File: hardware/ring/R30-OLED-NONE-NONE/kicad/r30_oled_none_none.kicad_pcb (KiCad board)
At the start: 2 copper layers, 43 x 18 mm, 32 parts, among them J1 USB4215-class 16P TH stakes, Q1 SI2301 P-FET, Q2 2N7002 gate driver, SW1 5mm 200gf dome, U1 ESP32-C3-MINI-1-N4, U2 PAW3204DB-TJ3L, U3 TP4054, U4 RT9080-33GJ5

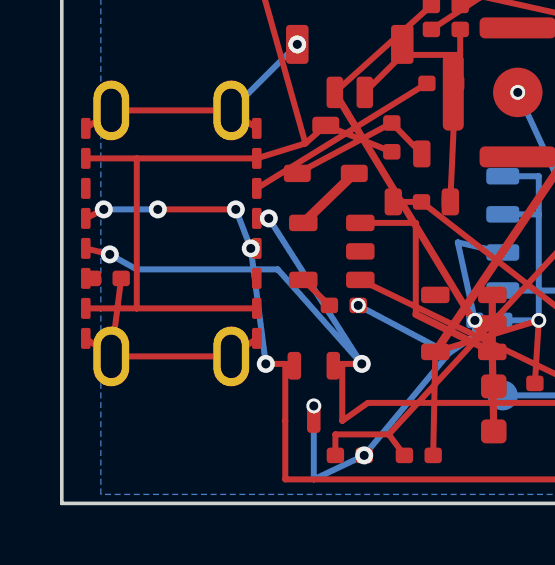
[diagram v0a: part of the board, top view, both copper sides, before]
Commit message: fix(r30): ease cc2 pulldown clearance
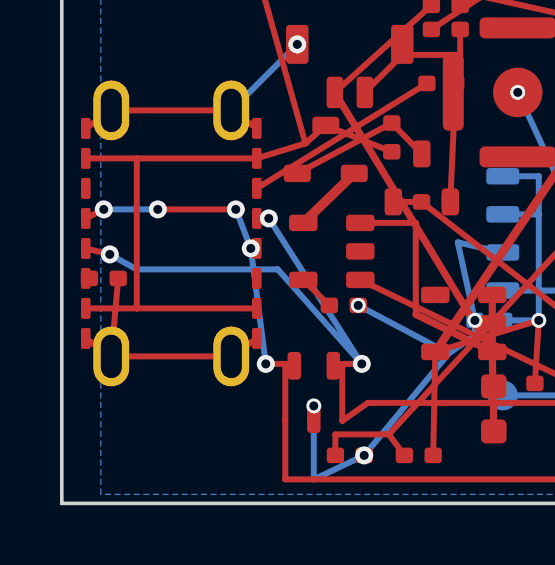
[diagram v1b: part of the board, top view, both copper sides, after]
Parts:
- moved R2B 0.10 mm to (100.4, 101.5)
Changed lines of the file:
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@@
   (footprint "Resistor_SMD:R_0402_1005Metric"
     (layer "F.Cu")
-    (at 100.500 101.500 0)
+    (at 100.400 101.500 0)
     (property "Reference" "R2B" (at 0 -1.05 0) (layer "F.Fab") (effects (font (size 0.6 0.6) (thickness 0.09))))
     (property "Value" "5.1k" (at 0 1.05 0) (layer "F.Fab") (effects (font (size 0.55 0.55) (thickness 0.08))))
@@
   (segment (start 119.600 108.200) (end 119.600 106.350) (width 0.20) (layer "F.Cu") (net 17))
   (segment (start 105.500 98.500) (end 111.170 95.000) (width 0.20) (layer "F.Cu") (net 18))
-  (segment (start 99.800 101.500) (end 100.020 101.500) (width 0.20) (layer "F.Cu") (net 19))
+  (segment (start 99.800 101.500) (end 99.920 101.500) (width 0.20) (layer "F.Cu") (net 19))
   (segment (start 108.950 101.550) (end 116.100 105.000) (width 0.20) (layer "F.Cu") (net 20))
   (segment (start 112.280 92.400) (end 113.000 92.100) (width 0.20) (layer "F.Cu") (net 21))
@@
   (segment (start 112.130 95.000) (end 111.950 98.950) (width 0.20) (layer "F.Cu") (net 1))
   (segment (start 108.880 102.400) (end 111.900 104.000) (width 0.20) (layer "B.Cu") (net 1))
-  (segment (start 100.980 101.500) (end 100.650 104.100) (width 0.20) (layer "F.Cu") (net 1))
+  (segment (start 100.880 101.500) (end 100.650 104.100) (width 0.20) (layer "F.Cu") (net 1))
   (segment (start 109.080 107.400) (end 111.900 104.000) (width 0.20) (layer "B.Cu") (net 1))
   (segment (start 111.900 104.000) (end 112.770 103.400) (width 0.20) (layer "B.Cu") (net 1))

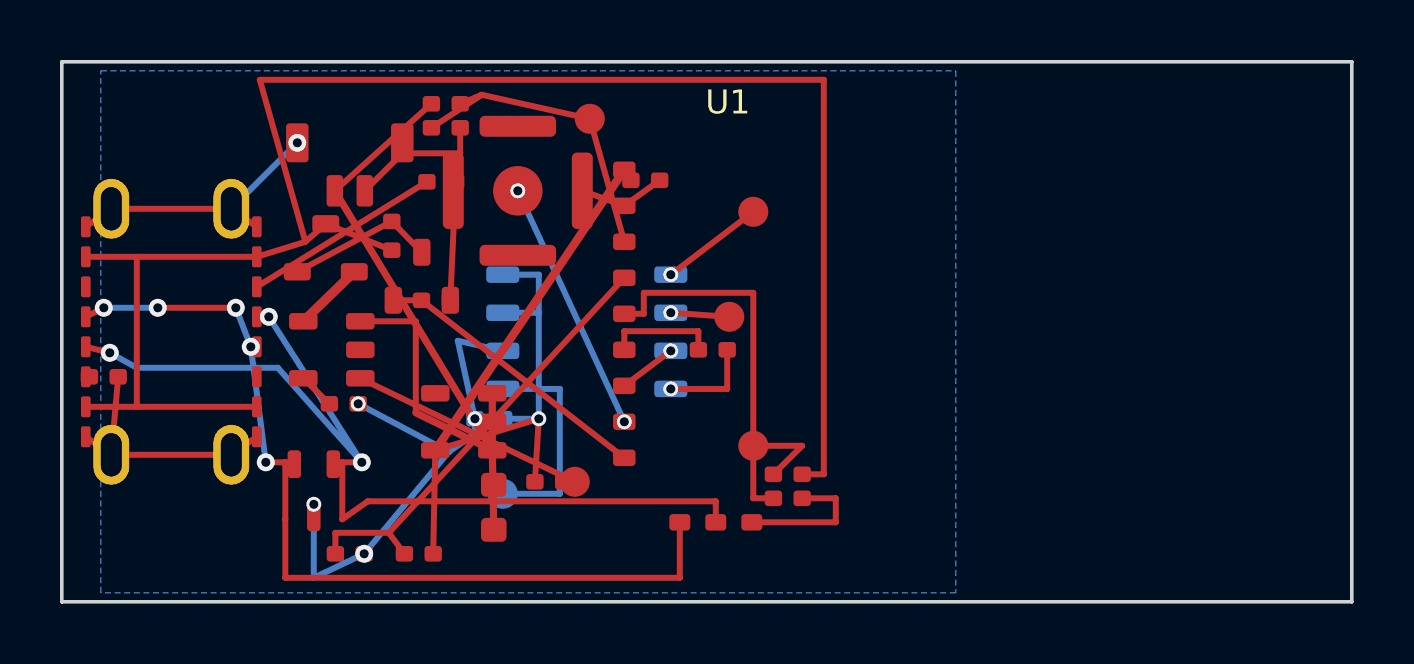
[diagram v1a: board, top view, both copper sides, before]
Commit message: fix(r30): ease dome switch clearance
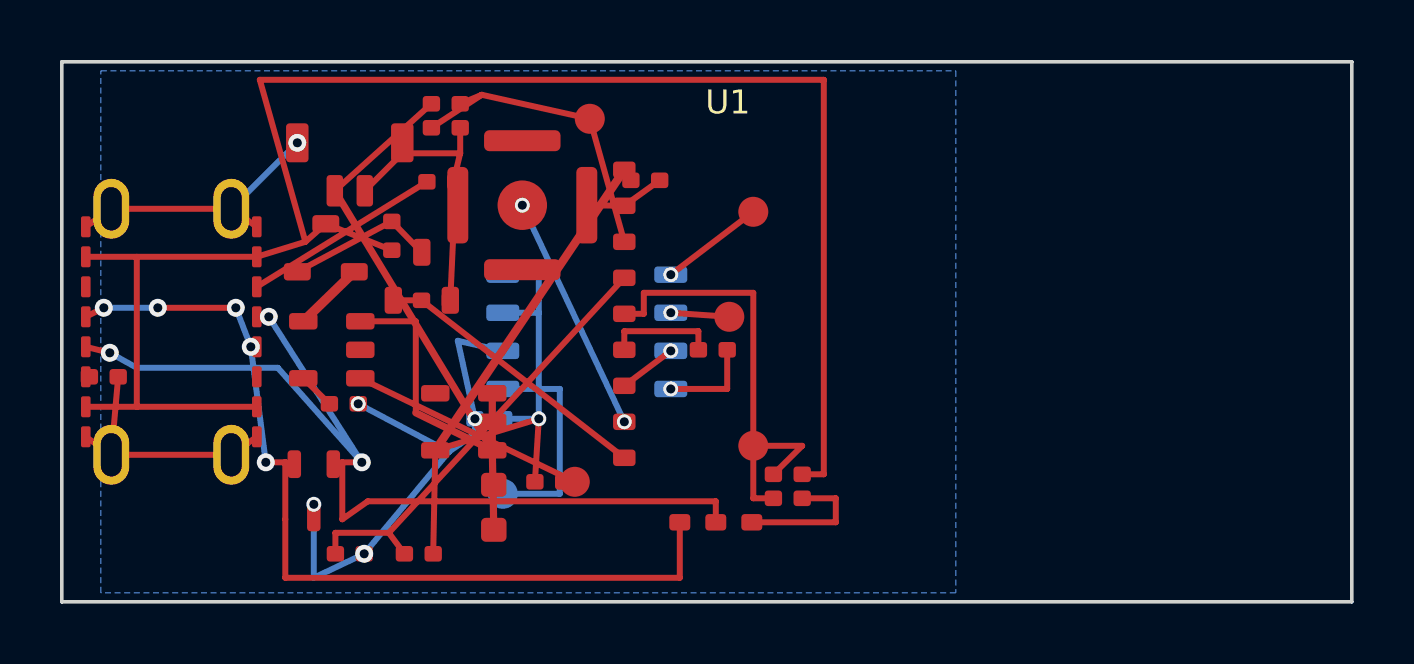
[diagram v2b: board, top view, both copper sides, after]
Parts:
- moved SW1 0.50 mm to (114.3, 95.8)
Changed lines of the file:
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@@
   (footprint "PowerFinger_Ring:Snap_Dome_5mm_TwoPad_Serviceable"
     (layer "F.Cu")
-    (at 114.200 95.300 0)
+    (at 114.350 95.780 0)
     (descr "5 mm metal snap dome contacts; accessible click zone")
     (property "Reference" "SW1" (at 0 -3.05 0) (layer "F.Fab") (effects (font (size 0.75 0.75) (thickness 0.11))))
@@
   (segment (start 124.800 106.350) (end 122.000 106.350) (width 0.20) (layer "F.Cu") (net 1))
   (segment (start 118.930 94.950) (end 117.750 95.800) (width 0.20) (layer "F.Cu") (net 1))
-  (segment (start 116.350 95.300) (end 117.750 95.800) (width 0.20) (layer "F.Cu") (net 1))
+  (segment (start 116.500 95.780) (end 117.750 95.800) (width 0.20) (layer "F.Cu") (net 1))
   (segment (start 114.770 105.000) (end 114.900 102.900) (width 0.20) (layer "F.Cu") (net 5))
   (segment (start 115.730 105.000) (end 116.100 105.000) (width 0.20) (layer "F.Cu") (net 20))
@@
   (segment (start 119.300 99.365) (end 121.250 99.500) (width 0.20) (layer "F.Cu") (net 13))
   (segment (start 119.300 98.095) (end 122.050 96.000) (width 0.20) (layer "F.Cu") (net 14))
-  (segment (start 114.200 95.300) (end 117.750 103.000) (width 0.20) (layer "B.Cu") (net 15))
+  (segment (start 114.350 95.780) (end 117.750 103.000) (width 0.20) (layer "B.Cu") (net 15))
   (segment (start 99.800 100.500) (end 100.600 100.700) (width 0.20) (layer "F.Cu") (net 16))
   (segment (start 100.600 100.700) (end 101.500 101.200) (width 0.20) (layer "B.Cu") (net 16))
@@
   (via (at 102.200 99.200) (size 0.60) (drill 0.30) (layers "F.Cu" "B.Cu") (net 17))
   (via (at 104.800 99.200) (size 0.60) (drill 0.30) (layers "F.Cu" "B.Cu") (net 17))
-  (via (at 114.200 95.300) (size 0.50) (drill 0.30) (layers "F.Cu" "B.Cu") (net 15))
+  (via (at 114.350 95.780) (size 0.50) (drill 0.30) (layers "F.Cu" "B.Cu") (net 15))
   (via (at 117.750 103.000) (size 0.50) (drill 0.30) (layers "F.Cu" "B.Cu") (net 15))
 )

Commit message: feat(r30): cut service hardware blockers
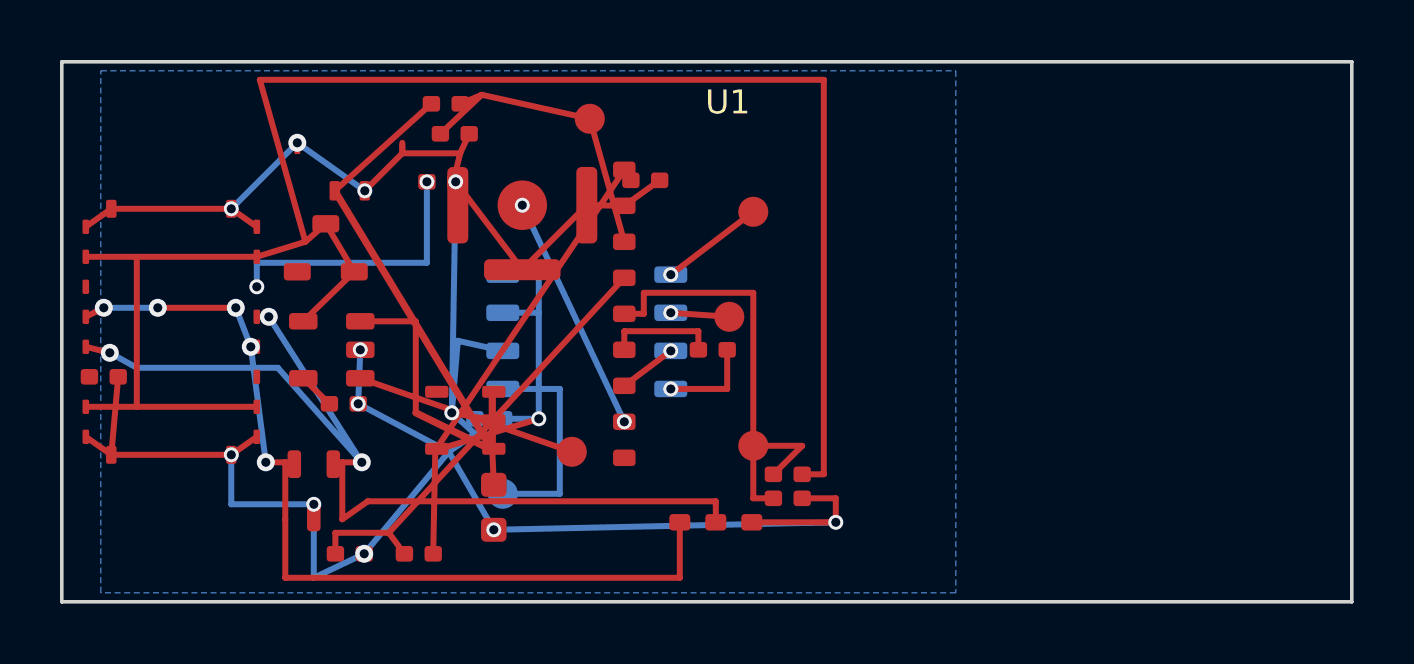
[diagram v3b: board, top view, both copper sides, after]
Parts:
- removed Q2: 2N7002 gate driver, Package_TO_SOT_SMD:SOT-23
- removed R11, R4, R6: 100k, Resistor_SMD:R_0402_1005Metric
- J1: value USB4215-class 16P TH stakes -> off-board USB service pads; footprint PowerFinger_Ring:USB_C_Receptacle_GCT_USB4215_Class_16P_TH_Stakes -> PowerFinger_Ring:Offboard_USB_Service_SameNet
- J_BAT: value SM02B-SRSS-TB class -> off-board battery service pads; footprint PowerFinger_Ring:JST_SH_SM02B-SRSS-TB_RA_1x02_P1.00mm -> PowerFinger_Ring:Offboard_Battery_Service_SameNet
- Q1: value SI2301 P-FET -> VBUS service jumper; footprint Package_TO_SOT_SMD:SOT-23 -> PowerFinger_Ring:VBUS_Service_Jumper_SOT23Land
- TP_CHRG: value CHRG_STAT pulled-up status pad -> CHRG_STAT fixture status pad; footprint TestPoint:TestPoint_Pad_D1.0mm -> PowerFinger_Ring:TestPoint_Pad_D1.0mm_FirstBoard
- U4: footprint Package_TO_SOT_SMD:SOT-23-5 -> PowerFinger_Ring:RT9080_33GJ5_SOT23_5_ServiceClearance
- moved TP_CHRG 1.00 mm to (116.0, 104.0)
- moved R8 0.36 mm to (112.1, 93.4)
- moved U4 0.07 mm to (112.5, 103.0)
- turned C2 to 270 degrees
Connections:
- Q1 pad 1: CHARGE_GATE -> (no net)
- Q1 pad 2: VBUS_CHG_SW -> VBUS_5V
- U1 pad GPIO10: CHARGE_EN -> (no net)
- U3 pad 4: VBUS_CHG_SW -> VBUS_5V
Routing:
- net GND: track 53.6 -> 89.0 mm, vias 5 -> 12
- net CHARGE_EN: track 9.50 -> 0.00 mm
- net CHARGE_GATE: track 5.01 -> 0.00 mm
- net USB_CC1_RD: track 6.66 -> 9.17 mm, vias 0 -> 2
- net VBUS_CHG_SW: track 2.37 -> 0.00 mm
- net VREG_3V3: track 29.2 -> 27.1 mm
- net VBUS_5V: track 59.7 -> 61.5 mm
- net VBAT_PROTECTED: track 26.7 -> 25.2 mm
- net CHRG_STAT: track 8.31 -> 7.46 mm

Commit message: fix(r30): move service shield return off vbus
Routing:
- net GND: vias 12 -> 14
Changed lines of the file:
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@@
   (segment (start 112.050 95.000) (end 112.130 95.000) (width 0.20) (layer "F.Cu") (net 1))
   (segment (start 108.880 102.400) (end 111.900 104.000) (width 0.20) (layer "B.Cu") (net 1))
-  (segment (start 100.880 101.500) (end 100.650 104.100) (width 0.20) (layer "F.Cu") (net 1))
+  (segment (start 100.880 101.500) (end 100.650 104.100) (width 0.20) (layer "B.Cu") (net 1))
   (segment (start 109.080 107.400) (end 111.900 104.000) (width 0.20) (layer "B.Cu") (net 1))
   (segment (start 111.900 104.000) (end 112.770 103.400) (width 0.20) (layer "B.Cu") (net 1))
@@
   (via (at 124.800 106.350) (size 0.50) (drill 0.30) (layers "F.Cu" "B.Cu") (net 1))
   (via (at 104.650 104.100) (size 0.50) (drill 0.30) (layers "F.Cu" "B.Cu") (net 1))
+  (via (at 100.880 101.500) (size 0.50) (drill 0.30) (layers "F.Cu" "B.Cu") (net 1))
+  (via (at 100.650 104.100) (size 0.50) (drill 0.30) (layers "F.Cu" "B.Cu") (net 1))
   (via (at 114.900 102.900) (size 0.50) (drill 0.30) (layers "F.Cu" "B.Cu") (net 5))
   (segment (start 113.400 102.950) (end 112.000 102.700) (width 0.20) (layer "F.Cu") (net 1))

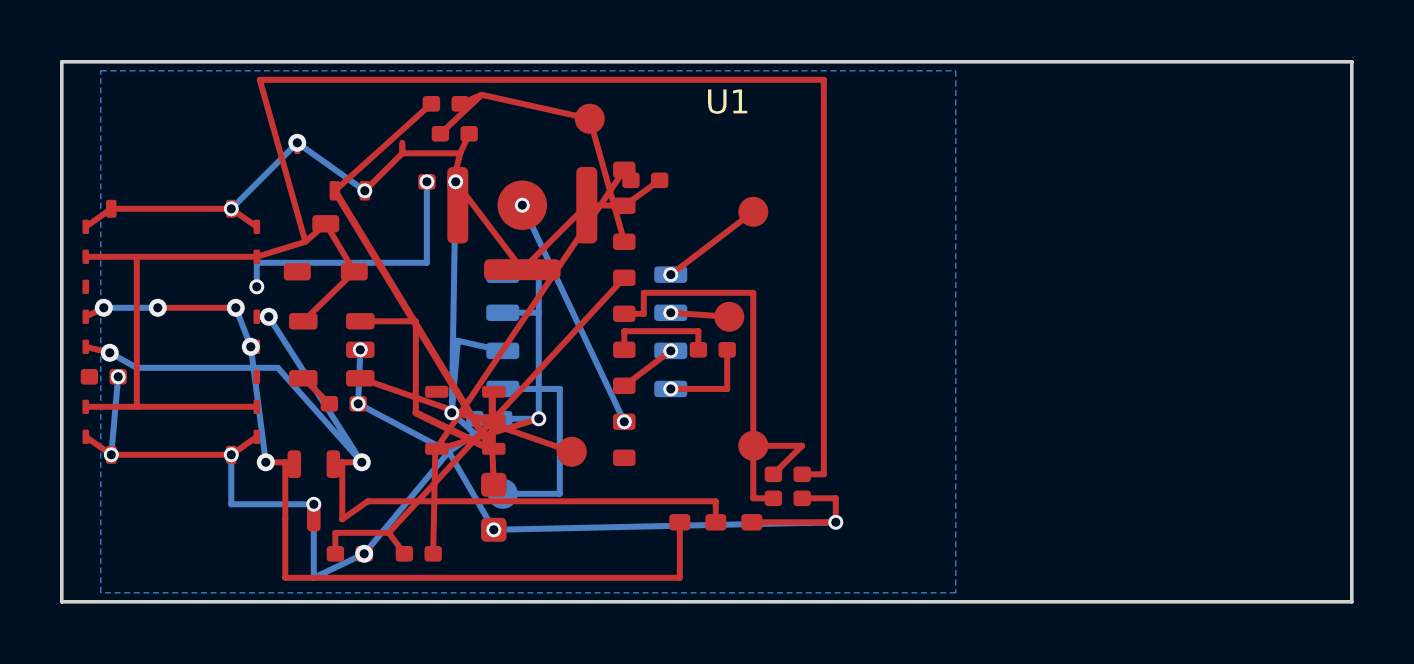
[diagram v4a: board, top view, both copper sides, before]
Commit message: fix(r30): retarget charge status endpoint
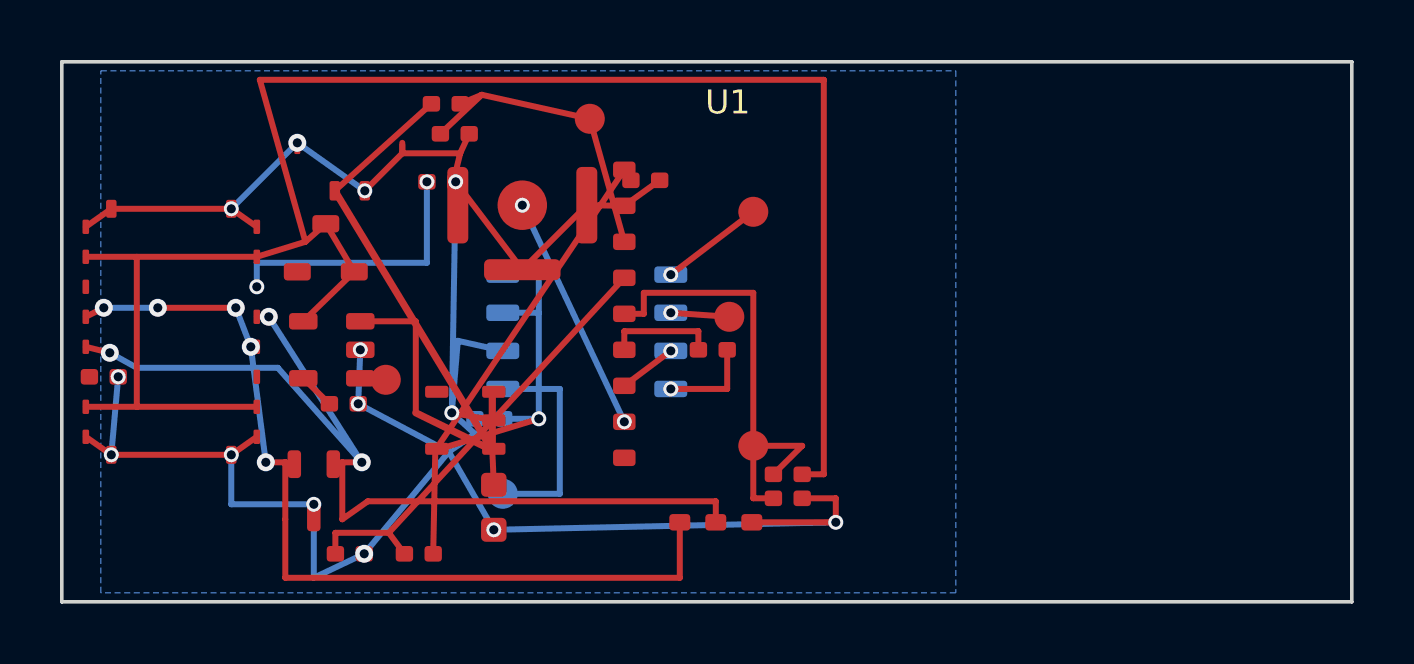
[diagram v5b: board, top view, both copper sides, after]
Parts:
- moved TP_CHRG 6.65 mm to (109.8, 101.6)
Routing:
- net CHRG_STAT: track 7.46 -> 0.85 mm
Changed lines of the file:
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@@
   (footprint "PowerFinger_Ring:TestPoint_Pad_D1.0mm_FirstBoard"
     (layer "F.Cu")
-    (at 116.000 104.000 0)
+    (at 109.800 101.600 0)
     (attr exclude_from_bom)
     (property "Reference" "TP_CHRG" (at 0 -1.20 0) (layer "F.Fab") (effects (font (size 0.55 0.55) (thickness 0.08))))
@@
   (segment (start 119.600 108.200) (end 119.600 106.350) (width 0.20) (layer "F.Cu") (net 17))
   (segment (start 99.800 101.500) (end 99.920 101.500) (width 0.20) (layer "F.Cu") (net 19))
-  (segment (start 108.950 101.550) (end 116.000 104.000) (width 0.20) (layer "F.Cu") (net 20))
+  (segment (start 108.950 101.550) (end 109.800 101.600) (width 0.20) (layer "F.Cu") (net 20))
   (segment (start 112.280 92.400) (end 113.000 92.100) (width 0.20) (layer "F.Cu") (net 21))
   (segment (start 111.620 93.400) (end 113.000 92.100) (width 0.20) (layer "F.Cu") (net 21))

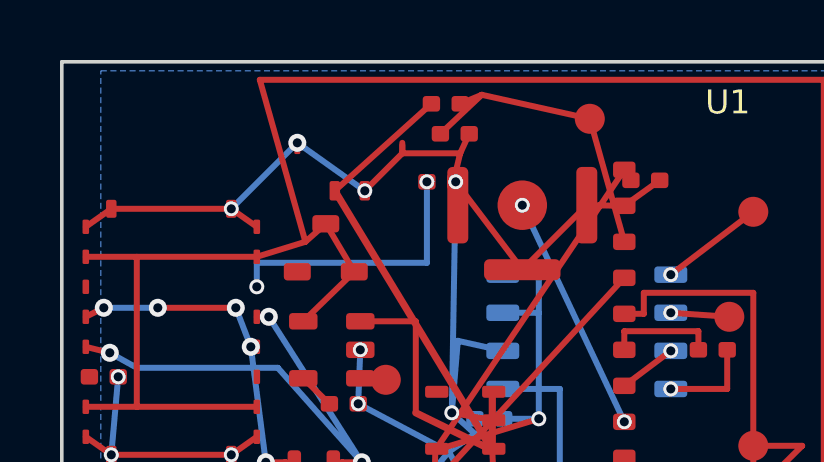
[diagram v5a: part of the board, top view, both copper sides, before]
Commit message: fix(r30): dogleg battery-service vbat feed
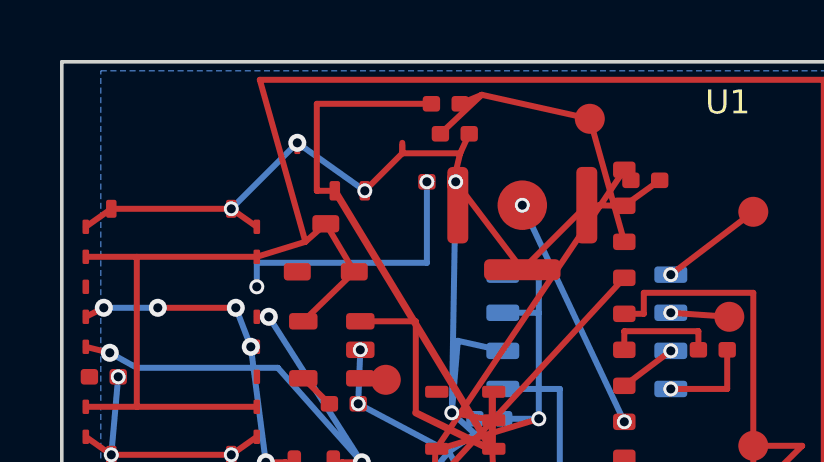
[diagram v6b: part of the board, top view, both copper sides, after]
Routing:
- net VBAT_PROTECTED: track 25.2 -> 28.2 mm
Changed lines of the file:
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@@
   (segment (start 112.200 100.300) (end 113.700 100.635) (width 0.20) (layer "B.Cu") (net 1))
   (segment (start 107.050 101.550) (end 107.920 102.400) (width 0.20) (layer "F.Cu") (net 6))
-  (segment (start 111.320 92.400) (end 108.100 95.300) (width 0.20) (layer "F.Cu") (net 4))
+  (segment (start 111.320 92.400) (end 107.500 92.400) (width 0.20) (layer "F.Cu") (net 4))
+  (segment (start 107.500 92.400) (end 107.500 95.300) (width 0.20) (layer "F.Cu") (net 4))
+  (segment (start 107.500 95.300) (end 108.100 95.300) (width 0.20) (layer "F.Cu") (net 4))
   (segment (start 112.580 93.400) (end 112.280 94.050) (width 0.20) (layer "F.Cu") (net 1))
   (segment (start 112.280 94.050) (end 110.350 94.050) (width 0.20) (layer "F.Cu") (net 1))
